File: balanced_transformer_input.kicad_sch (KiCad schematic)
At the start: 23 parts, among them J3 XLR3_Ground, Q5 SI2309CDS-T1-GE3, Q6 SS8050

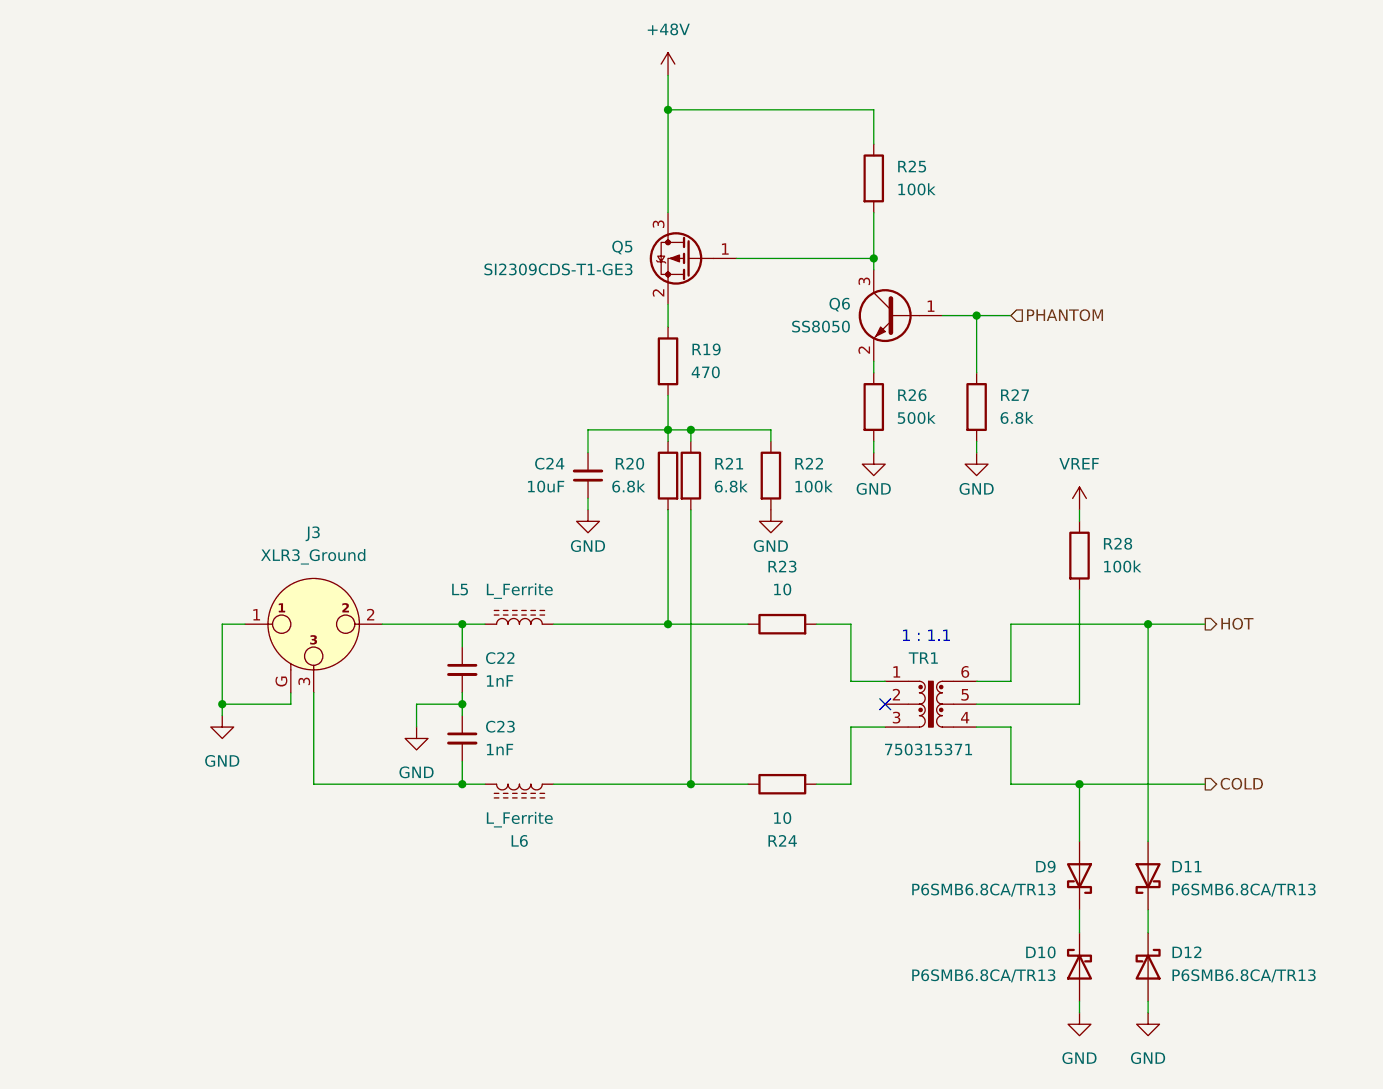
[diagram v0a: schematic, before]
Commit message: some suggested changes to the schematic:
- common pull-down mosfet for phantom power switch
- added board interconnect header
- proposed buffer for VREF
- cosmetic changes
- address selection jumpers
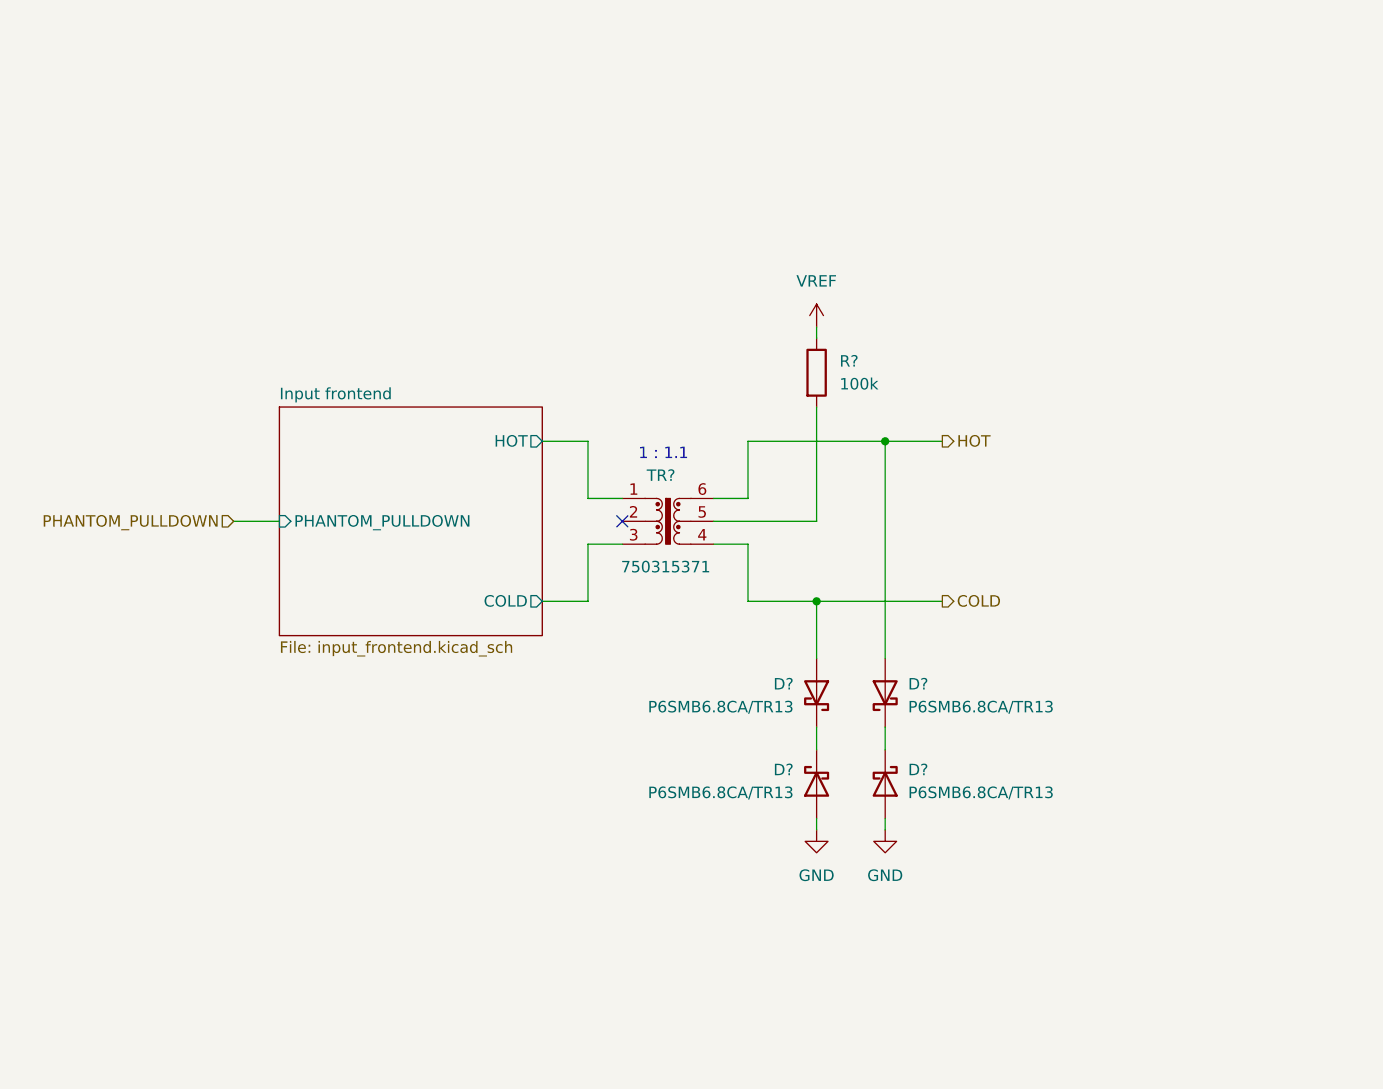
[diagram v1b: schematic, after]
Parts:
- removed C22, C23: 1nF, Capacitor_SMD:C_0603_1608Metric, symbol Device:C_Small
- removed C24: 10uF, Capacitor_SMD:C_0603_1608Metric, symbol Device:C_Small
- removed J3: XLR3_Ground, symbol Connector_Audio:XLR3_Ground
- removed L5, L6: L_Ferrite, symbol Device:L_Ferrite
- removed Q5: SI2309CDS-T1-GE3, Package_TO_SOT_SMD:SOT-23, symbol Transistor_FET:Si2371EDS
- removed Q6: SS8050, Package_TO_SOT_SMD:SOT-23, symbol Transistor_BJT:SS8050
- removed R19: 470, Resistor_SMD:R_0603_1608Metric, symbol Device:R
- removed R20, R21, R27: 6.8k, Resistor_SMD:R_0603_1608Metric, symbol Device:R
- removed R22, R25: 100k, Resistor_SMD:R_0603_1608Metric, symbol Device:R
- removed R23, R24: 10, Resistor_SMD:R_0603_1608Metric, symbol Device:R
- removed R26: 500k, Resistor_SMD:R_0603_1608Metric, symbol Device:R
- renumbered D12 to D?, D10 to D?, D11 to D?, D9 to D?, R28 to R?, TR1 to TR?
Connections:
- net Input frontend/HOT: now reaches TR?.1
- net Input frontend/COLD: now reaches TR?.3
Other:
- added sheet Input frontend (input_frontend.kicad_sch)
- moved on the sheet: D?, R?, TR?

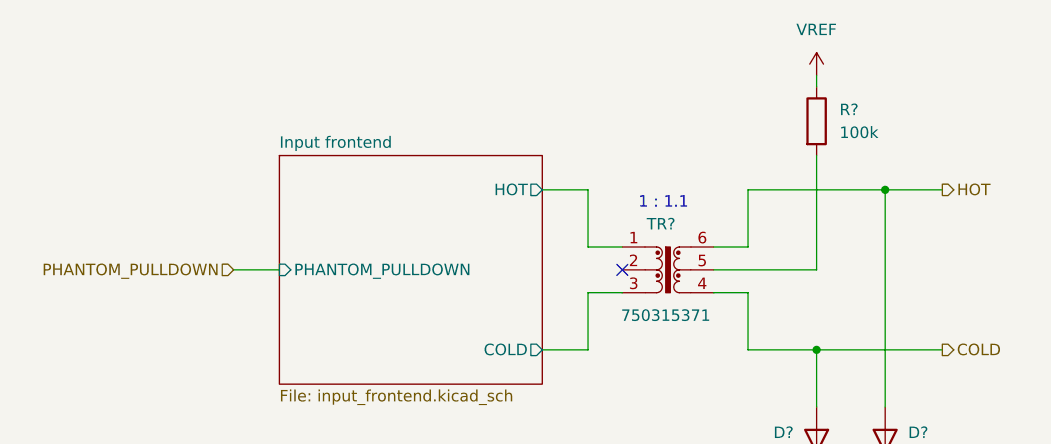
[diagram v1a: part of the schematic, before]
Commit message: independent phantom control and removed transformer bias
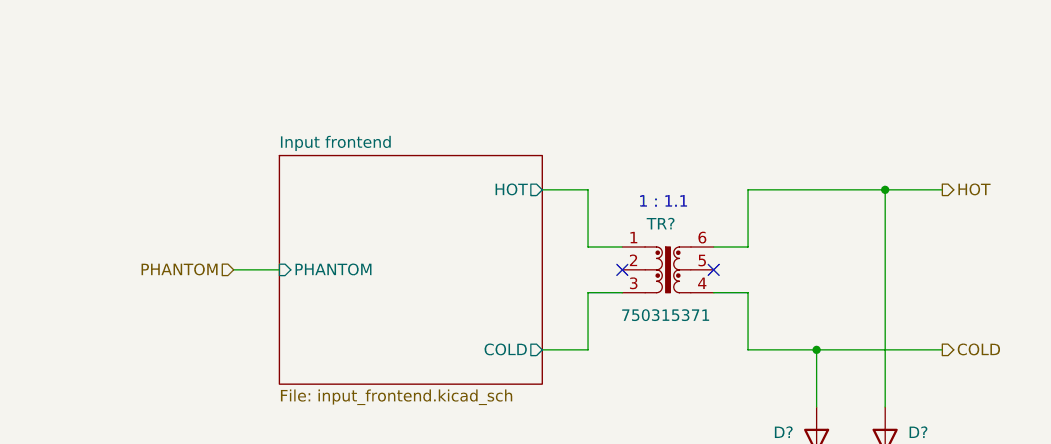
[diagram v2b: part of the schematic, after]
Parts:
- removed R?: 100k, Resistor_SMD:R_0603_1608Metric, symbol Device:R
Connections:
- no-connect marks 1 -> 2
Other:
- sheet Input frontend ports: added PHANTOM; removed PHANTOM_PULLDOWN
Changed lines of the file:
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@@
 		(at 128.27 91.44)
 	)
+	(no_connect
+		(at 138.43 91.44)
+	)
 	(wire
 		(pts
@@
 	(wire
 		(pts
-			(xy 149.86 69.85) (xy 149.86 71.12)
-		)
-		(stroke
-			(width 0)
-			(type default)
-		)
-	)
-	(wire
-		(pts
 			(xy 142.24 88.9) (xy 142.24 82.55)
 		)
@@
 	(wire
 		(pts
-			(xy 138.43 91.44) (xy 149.86 91.44)
-		)
-		(stroke
-			(width 0)
-			(type default)
-		)
-	)
-	(wire
-		(pts
 			(xy 119.38 100.33) (xy 124.46 100.33)
 		)
@@
 	(wire
 		(pts
-			(xy 149.86 91.44) (xy 149.86 78.74)
-		)
-		(stroke
-			(width 0)
-			(type default)
-		)
-	)
-	(wire
-		(pts
 			(xy 157.48 82.55) (xy 163.83 82.55)
 		)
@@
 			(width 0)
 			(type default)
+		)
+	)
+	(hierarchical_label "PHANTOM"
+		(shape input)
+		(at 85.09 91.44 180)
+		(effects
+			(font
+				(size 1.27 1.27)
+			)
+			(justify right)
 		)
 	)
@@
 			)
 			(justify left)
-		)
-	)
-	(hierarchical_label "PHANTOM_PULLDOWN"
-		(shape input)
-		(at 85.09 91.44 180)
-		(effects
-			(font
-				(size 1.27 1.27)
-			)
-			(justify right)
 		)
 	)
@@
 	)
 	(symbol
-		(lib_id "Device:R")
-		(at 149.86 74.93 0)
-		(unit 1)
-		(exclude_from_sim no)
-		(in_bom yes)
-		(on_board yes)
-		(dnp no)
-		(fields_autoplaced yes)
-		(property "Reference" "R?"
-			(at 152.4 73.6599 0)
-			(effects
-				(font
-					(size 1.27 1.27)
-				)
-				(justify left)
-			)
-		)
-		(property "Value" "100k"
-			(at 152.4 76.1999 0)
-			(effects
-				(font
-					(size 1.27 1.27)
-				)
-				(justify left)
-			)
-		)
-		(property "Footprint" "Resistor_SMD:R_0603_1608Metric"
-			(at 148.082 74.93 90)
-			(effects
-				(font
-					(size 1.27 1.27)
-				)
-				(hide yes)
-			)
-		)
-		(property "Datasheet" "~"
-			(at 149.86 74.93 0)
-			(effects
-				(font
-					(size 1.27 1.27)
-				)
-				(hide yes)
-			)
-		)
-		(property "Description" "Resistor"
-			(at 149.86 74.93 0)
-			(effects
-				(font
-					(size 1.27 1.27)
-				)
-				(hide yes)
-			)
-		)
-		(pin "2"
-		)
-		(pin "1"
-		)
-		(instances
-			(project "mv2_taa3040"
-				(path "/41a55a1d-5108-482f-b313-9eaa5d011dff/1c3f6b07-c9aa-4f11-804b-09faf49e24ef"
-					(reference "R?")
-					(unit 1)
-				)
-				(path "/41a55a1d-5108-482f-b313-9eaa5d011dff/bd2f1d91-73ea-4344-9315-80da99bbdd84"
-					(reference "R28")
-					(unit 1)
-				)
-			)
-		)
-	)
-	(symbol
 		(lib_id "Device:D_Schottky")
 		(at 149.86 120.65 90)
@@
 				(path "/41a55a1d-5108-482f-b313-9eaa5d011dff/bd2f1d91-73ea-4344-9315-80da99bbdd84"
 					(reference "D11")
-					(unit 1)
-				)
-			)
-		)
-	)
-	(symbol
-		(lib_id "power:VDC")
-		(at 149.86 69.85 0)
-		(unit 1)
-		(exclude_from_sim no)
-		(in_bom yes)
-		(on_board yes)
-		(dnp no)
-		(fields_autoplaced yes)
-		(property "Reference" "#PWR024"
-			(at 149.86 73.66 0)
-			(effects
-				(font
-					(size 1.27 1.27)
-				)
-				(hide yes)
-			)
-		)
-		(property "Value" "VREF"
-			(at 149.86 64.77 0)
-			(effects
-				(font
-					(size 1.27 1.27)
-				)
-			)
-		)
-		(property "Footprint" ""
-			(at 149.86 69.85 0)
-			(effects
-				(font
-					(size 1.27 1.27)
-				)
-				(hide yes)
-			)
-		)
-		(property "Datasheet" ""
-			(at 149.86 69.85 0)
-			(effects
-				(font
-					(size 1.27 1.27)
-				)
-				(hide yes)
-			)
-		)
-		(property "Description" "Power symbol creates a global label with name \"VDC\""
-			(at 149.86 69.85 0)
-			(effects
-				(font
-					(size 1.27 1.27)
-				)
-				(hide yes)
-			)
-		)
-		(pin "1"
-		)
-		(instances
-			(project "mv2_taa3040"
-				(path "/41a55a1d-5108-482f-b313-9eaa5d011dff/1c3f6b07-c9aa-4f11-804b-09faf49e24ef"
-					(reference "#PWR024")
-					(unit 1)
-				)
-				(path "/41a55a1d-5108-482f-b313-9eaa5d011dff/bd2f1d91-73ea-4344-9315-80da99bbdd84"
-					(reference "#PWR043")
 					(unit 1)
 				)
@@
 			)
 		)
-		(pin "PHANTOM_PULLDOWN" input
+		(pin "PHANTOM" input
 			(at 90.17 91.44 180)
 			(effects

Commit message: assign some component data
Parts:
- D10, D11, D12, D9: renamed from D?; MPN (none) -> P6SMB6.8CA/TR13
- gave numbers to parts that had none: 1
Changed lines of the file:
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@@
 		(on_board yes)
 		(dnp no)
-		(property "Reference" "D?"
+		(property "Reference" "D12"
 			(at 160.02 119.0624 90)
 			(effects
@@
 		)
 		(property "LCSC" "C78395"
+			(at 157.48 120.65 90)
+			(effects
+				(font
+					(size 1.27 1.27)
+				)
+				(hide yes)
+			)
+		)
+		(property "MPN" "P6SMB6.8CA/TR13"
 			(at 157.48 120.65 90)
 			(effects
@@
 			(project "mv2_taa3040"
 				(path "/41a55a1d-5108-482f-b313-9eaa5d011dff/1c3f6b07-c9aa-4f11-804b-09faf49e24ef"
-					(reference "D?")
+					(reference "D12")
 					(unit 1)
 				)
 				(path "/41a55a1d-5108-482f-b313-9eaa5d011dff/bd2f1d91-73ea-4344-9315-80da99bbdd84"
-					(reference "D12")
+					(reference "D16")
 					(unit 1)
 				)
@@
 		(on_board yes)
 		(dnp no)
-		(property "Reference" "TR?"
+		(property "Reference" "TR1"
 			(at 132.588 86.36 0)
 			(effects
@@
 			(project "mv2_taa3040"
 				(path "/41a55a1d-5108-482f-b313-9eaa5d011dff/1c3f6b07-c9aa-4f11-804b-09faf49e24ef"
-					(reference "TR?")
+					(reference "TR1")
 					(unit 1)
 				)
 				(path "/41a55a1d-5108-482f-b313-9eaa5d011dff/bd2f1d91-73ea-4344-9315-80da99bbdd84"
-					(reference "TR1")
+					(reference "TR2")
 					(unit 1)
 				)
@@
 		(dnp no)
 		(fields_autoplaced yes)
-		(property "Reference" "#PWR026"
+		(property "Reference" "#PWR047"
 			(at 157.48 132.08 0)
 			(effects
@@
 			(project "mv2_taa3040"
 				(path "/41a55a1d-5108-482f-b313-9eaa5d011dff/1c3f6b07-c9aa-4f11-804b-09faf49e24ef"
-					(reference "#PWR026")
+					(reference "#PWR047")
 					(unit 1)
 				)
 				(path "/41a55a1d-5108-482f-b313-9eaa5d011dff/bd2f1d91-73ea-4344-9315-80da99bbdd84"
-					(reference "#PWR042")
+					(reference "#PWR056")
 					(unit 1)
 				)
@@
 		(dnp no)
 		(fields_autoplaced yes)
-		(property "Reference" "#PWR025"
+		(property "Reference" "#PWR046"
 			(at 149.86 132.08 0)
 			(effects
@@
 			(project "mv2_taa3040"
 				(path "/41a55a1d-5108-482f-b313-9eaa5d011dff/1c3f6b07-c9aa-4f11-804b-09faf49e24ef"
-					(reference "#PWR025")
+					(reference "#PWR046")
 					(unit 1)
 				)
 				(path "/41a55a1d-5108-482f-b313-9eaa5d011dff/bd2f1d91-73ea-4344-9315-80da99bbdd84"
-					(reference "#PWR040")
+					(reference "#PWR055")
 					(unit 1)
 				)
@@
 		(on_board yes)
 		(dnp no)
-		(property "Reference" "D?"
+		(property "Reference" "D10"
 			(at 147.32 119.0624 90)
 			(effects
@@
 		)
 		(property "LCSC" "C78395"
+			(at 149.86 120.65 90)
+			(effects
+				(font
+					(size 1.27 1.27)
+				)
+				(hide yes)
+			)
+		)
+		(property "MPN" "P6SMB6.8CA/TR13"
 			(at 149.86 120.65 90)
 			(effects
@@
 			(project "mv2_taa3040"
 				(path "/41a55a1d-5108-482f-b313-9eaa5d011dff/1c3f6b07-c9aa-4f11-804b-09faf49e24ef"
-					(reference "D?")
+					(reference "D10")
 					(unit 1)
 				)
 				(path "/41a55a1d-5108-482f-b313-9eaa5d011dff/bd2f1d91-73ea-4344-9315-80da99bbdd84"
-					(reference "D10")
+					(reference "D14")
 					(unit 1)
 				)
@@
 		(on_board yes)
 		(dnp no)
-		(property "Reference" "D?"
+		(property "Reference" "D11"
 			(at 160.02 109.5374 90)
 			(effects
@@
 		)
 		(property "LCSC" "C78395"
+			(at 157.48 110.49 90)
+			(effects
+				(font
+					(size 1.27 1.27)
+				)
+				(hide yes)
+			)
+		)
+		(property "MPN" "P6SMB6.8CA/TR13"
 			(at 157.48 110.49 90)
 			(effects
@@
 			(project "mv2_taa3040"
 				(path "/41a55a1d-5108-482f-b313-9eaa5d011dff/1c3f6b07-c9aa-4f11-804b-09faf49e24ef"
-					(reference "D?")
+					(reference "D11")
 					(unit 1)
 				)
 				(path "/41a55a1d-5108-482f-b313-9eaa5d011dff/bd2f1d91-73ea-4344-9315-80da99bbdd84"
-					(reference "D11")
+					(reference "D15")
 					(unit 1)
 				)
@@
 		(on_board yes)
 		(dnp no)
-		(property "Reference" "D?"
+		(property "Reference" "D9"
 			(at 147.32 109.5374 90)
 			(effects
@@
 		)
 		(property "LCSC" "C78395"
+			(at 149.86 110.49 90)
+			(effects
+				(font
+					(size 1.27 1.27)
+				)
+				(hide yes)
+			)
+		)
+		(property "MPN" "P6SMB6.8CA/TR13"
 			(at 149.86 110.49 90)
 			(effects
@@
 			(project "mv2_taa3040"
 				(path "/41a55a1d-5108-482f-b313-9eaa5d011dff/1c3f6b07-c9aa-4f11-804b-09faf49e24ef"
-					(reference "D?")
+					(reference "D9")
 					(unit 1)
 				)
 				(path "/41a55a1d-5108-482f-b313-9eaa5d011dff/bd2f1d91-73ea-4344-9315-80da99bbdd84"
-					(reference "D9")
-					(unit 1)
-				)
+					(reference "D13")
+					(unit 1)
+				)

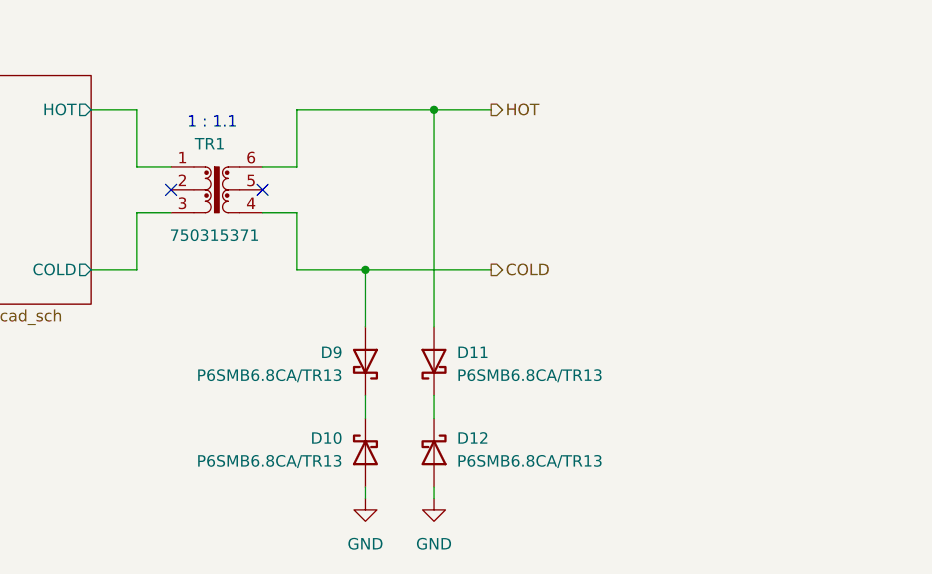
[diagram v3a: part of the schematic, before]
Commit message: tvs clamps
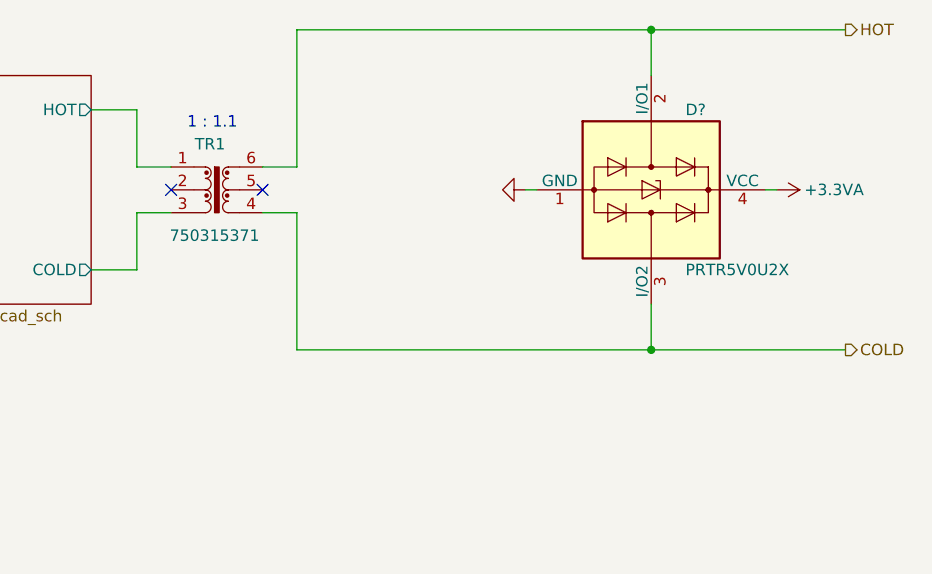
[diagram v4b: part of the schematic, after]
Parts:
- removed D10, D11, D12, D9: P6SMB6.8CA/TR13, Diode_SMD:D_SMB, symbol Device:D_Schottky
- added D?: PRTR5V0U2X, Package_TO_SOT_SMD:SOT-143, symbol Power_Protection:PRTR5V0U2X
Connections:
- net COLD: now also D?.3 (I/O2)
- net GND: now also D?.1 (GND)
- net HOT: now also D?.2 (I/O1)
- new net +3.3VA: D?.4 (VCC)

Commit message: some final touches
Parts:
- gave numbers to parts that had none: 1
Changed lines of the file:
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@@
 		(on_board yes)
 		(dnp no)
-		(property "Reference" "#PWR072"
+		(property "Reference" "#PWR038"
 			(at 191.77 91.44 0)
 			(effects
@@
 			(project "mv2_taa3040"
 				(path "/41a55a1d-5108-482f-b313-9eaa5d011dff/1c3f6b07-c9aa-4f11-804b-09faf49e24ef"
-					(reference "#PWR072")
+					(reference "#PWR038")
 					(unit 1)
 				)
 				(path "/41a55a1d-5108-482f-b313-9eaa5d011dff/bd2f1d91-73ea-4344-9315-80da99bbdd84"
-					(reference "#PWR074")
+					(reference "#PWR047")
 					(unit 1)
 				)
@@
 		(on_board yes)
 		(dnp no)
-		(property "Reference" "D?"
+		(property "Reference" "D3"
 			(at 185.42 82.55 90)
 			(effects
@@
 			(project "mv2_taa3040"
 				(path "/41a55a1d-5108-482f-b313-9eaa5d011dff/1c3f6b07-c9aa-4f11-804b-09faf49e24ef"
-					(reference "D?")
+					(reference "D3")
 					(unit 1)
 				)
 				(path "/41a55a1d-5108-482f-b313-9eaa5d011dff/bd2f1d91-73ea-4344-9315-80da99bbdd84"
-					(reference "D?")
+					(reference "D4")
 					(unit 1)
 				)
@@
 		(dnp no)
 		(fields_autoplaced yes)
-		(property "Reference" "#PWR071"
+		(property "Reference" "#PWR037"
 			(at 161.29 91.44 0)
 			(effects
@@
 			(project "mv2_taa3040"
 				(path "/41a55a1d-5108-482f-b313-9eaa5d011dff/1c3f6b07-c9aa-4f11-804b-09faf49e24ef"
-					(reference "#PWR071")
+					(reference "#PWR037")
 					(unit 1)
 				)
 				(path "/41a55a1d-5108-482f-b313-9eaa5d011dff/bd2f1d91-73ea-4344-9315-80da99bbdd84"
-					(reference "#PWR073")
-					(unit 1)
-				)
+					(reference "#PWR046")
+					(unit 1)
+				)
